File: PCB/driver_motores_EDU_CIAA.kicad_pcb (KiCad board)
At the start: 2 copper layers, 85 x 90 mm, 38 parts, among them P1 CONN_01X02, P2 CONN_01X04, P3 CONN_01X05, P4 CONN_01X05, Q1 AOD417, U1 PCA9685-TSSOP, U2 24C32, U3 TB6612FNG, U4 TB6612FNG

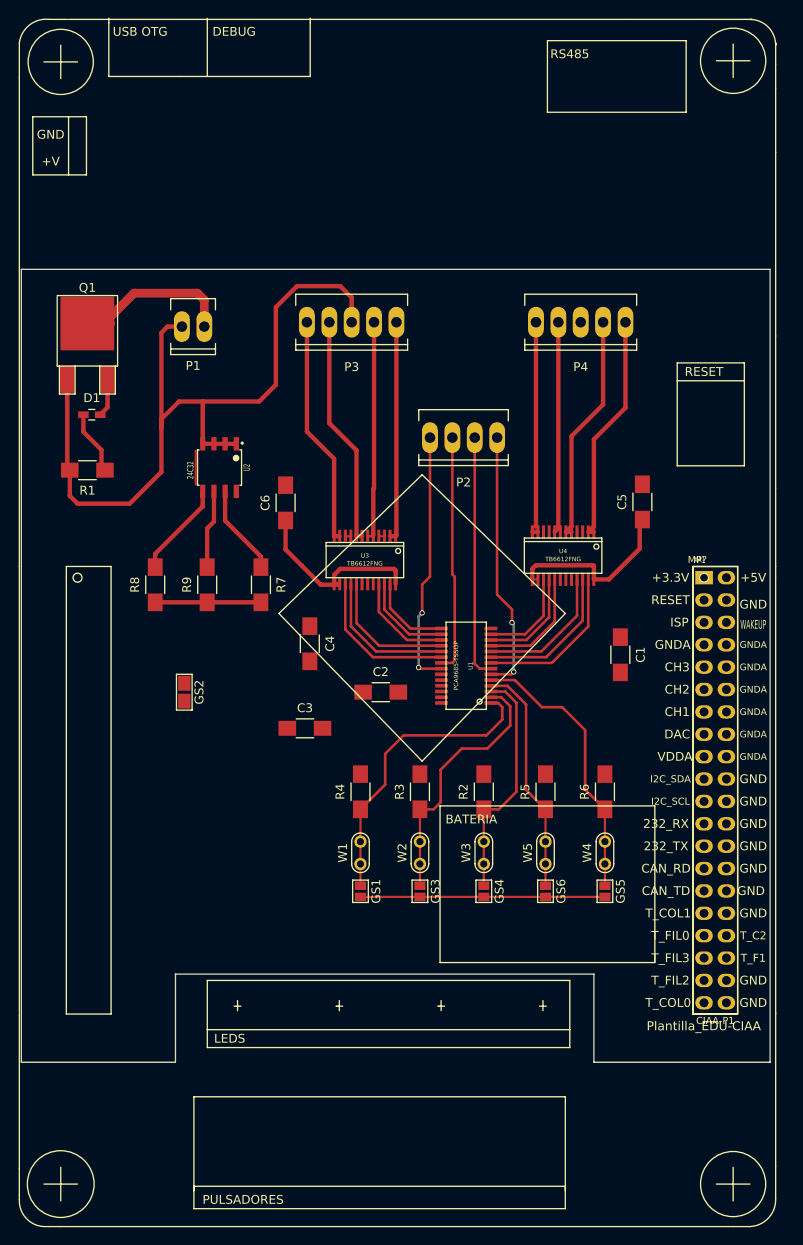
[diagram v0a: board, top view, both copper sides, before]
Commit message: termino ruteo, completo modulos 3D, modifico serigrafia
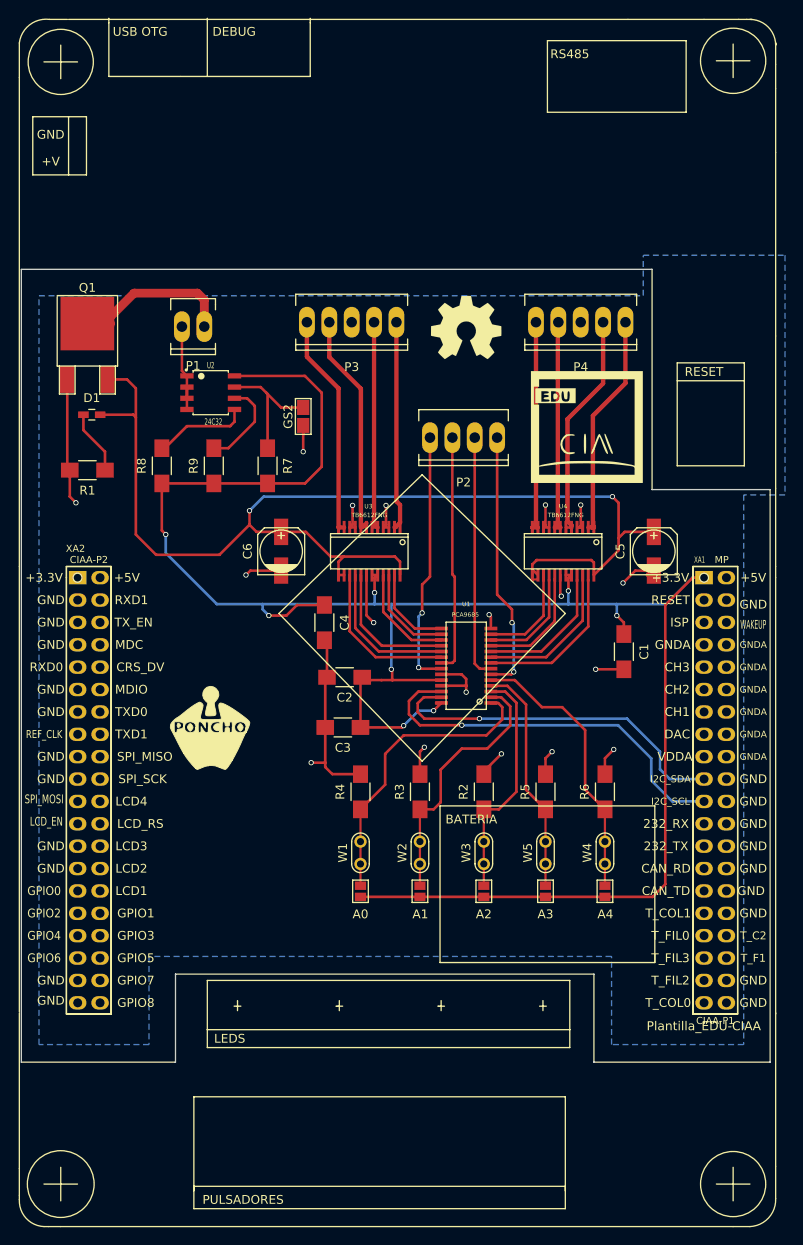
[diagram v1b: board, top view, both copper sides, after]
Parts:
- removed MP?: Plantilla_EDU-CIAA, ej2cese:Plantilla_EDU-CIAA
- added G***: LOGO, footprint:Logo_Poncho, F.Cu at (83.9, 107.1)
- added G***: Logo_EDU-CIAA, footprint:Logo_EDU-CIAA, F.Cu at (126.7, 72.9)
- added G101: Logo_OSHWA, footprint:Logo_OSHWA, F.Cu at (113.0, 61.6)
- added MP: Plantilla_EDU-CIAA, footprint:Plantilla_EDU-CIAA, F.Cu at (140.0, 90.0)
- added XA2: Conn_Poncho_Izquierdo, footprint:Conn_Poncho_Izquierdo, F.Cu at (68.9, 90.0)
- C5, C6: footprint tp_final:R_1206_HandSoldering -> Capacitors_SMD:c_elec_5x5.3
- U1: value PCA9685-TSSOP -> PCA9685
- moved GS2 34.1 mm to (94.5, 71.7), turned to 180 degrees
- moved R7 13.5 mm to (90.5, 77.3)
- moved R8 13.5 mm to (78.5, 77.3)
- moved R9 13.5 mm to (84.3, 77.3)
- moved U2 8.56 mm to (84.0, 69.0), turned to 0 degrees
- moved C5 5.75 mm to (134.3, 87.0)
- moved C6 5.52 mm to (92.0, 87.0)
- moved C2 4.44 mm to (99.2, 101.3), turned to 180 degrees
- moved C3 4.30 mm to (99.0, 107.0), turned to 180 degrees
- moved C4 2.91 mm to (96.9, 95.1)
- moved U3 1.12 mm to (102.0, 87.0)
- moved C1 0.53 mm to (130.9, 98.4)
- moved U4 0.50 mm to (124.0, 87.0)
- renumbered GS1 to A0, GS3 to A1, GS4 to A2, GS6 to A3, GS5 to A4
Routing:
- net +3V3: track 39.8 -> 238.7 mm, vias 0 -> 8
- net +12V: track 46.3 -> 131.9 mm, vias 0 -> 2
- net /SCL: track 0.00 -> 44.7 mm, vias 0 -> 1
- net /SDA: track 0.00 -> 40.8 mm, vias 0 -> 1
- net GND: track 93.5 -> 108.2 mm, vias 0 -> 18
- net Net-(GS2-Pad2): track 10.3 -> 15.4 mm
- net (no net): track 3.81 -> 0.00 mm
- net Net-(P3-Pad1): track 25.7 -> 23.8 mm
- net Net-(R9-Pad2): track 8.92 -> 10.4 mm
- net Net-(P3-Pad2): track 25.1 -> 24.2 mm
- net Net-(P3-Pad4): track 26.2 -> 25.4 mm
- net Net-(P3-Pad5): track 26.2 -> 25.4 mm
- net /LED11: track 15.2 -> 15.8 mm
- net /LED13: track 17.4 -> 18.0 mm
- net /LED12: track 16.3 -> 16.9 mm
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- added copper zone on B.Cu, net GND
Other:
- outline, holes or cut-outs redrawn

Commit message: se borran las carpetas sobrantes, completa el rotulo, se corrige el esquematico, se agrega serigrafia, se agrega tabla con las grillas
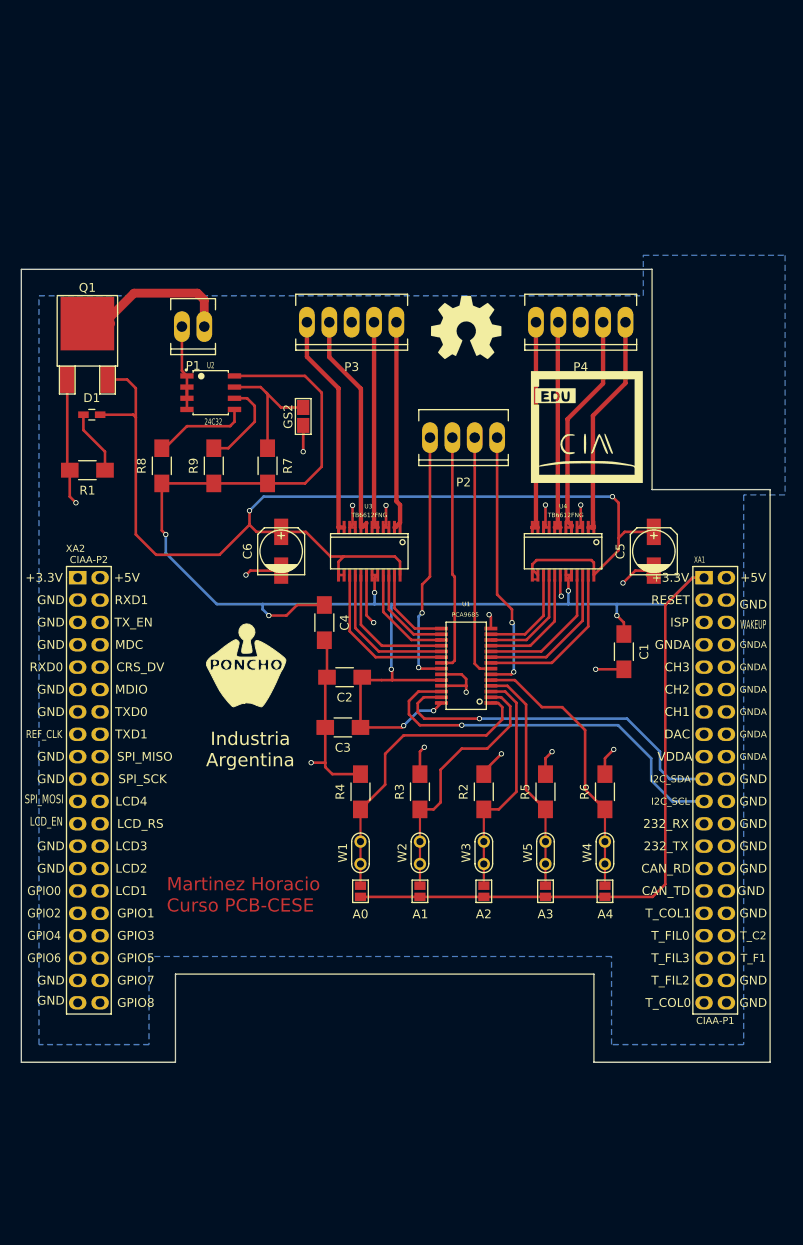
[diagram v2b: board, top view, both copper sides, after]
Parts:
- removed MP: Plantilla_EDU-CIAA, footprint:Plantilla_EDU-CIAA
- moved G*** 8.20 mm to (88.0, 100.0)
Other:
- net class Default: trace_width 0.25 -> 0.3; via_dia 0.6 -> 1.27; via_drill 0.4 -> 0.7
- net class net_power added: clearance 0.3, trace_width 0.75, via_dia 1.27, via_drill 0.7
- board text added: "Diseño doblefaz Sin requerimientos especiales Grilla de Ruteo: 0,1 mm Grilla de posicionamiento: 0,5 mm Ancho minimo de pista: 0,3 mm Diametro de agujero de via: 0,71 mm Diametro de via: 1,27mm"
- board text added: "Industria Argentina"
- board text added: "Martinez Horacio Curso PCB-CESE"
- board text added: "STACK-UP"

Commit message: se elimina carpeta DOC, se agregan serigrafias
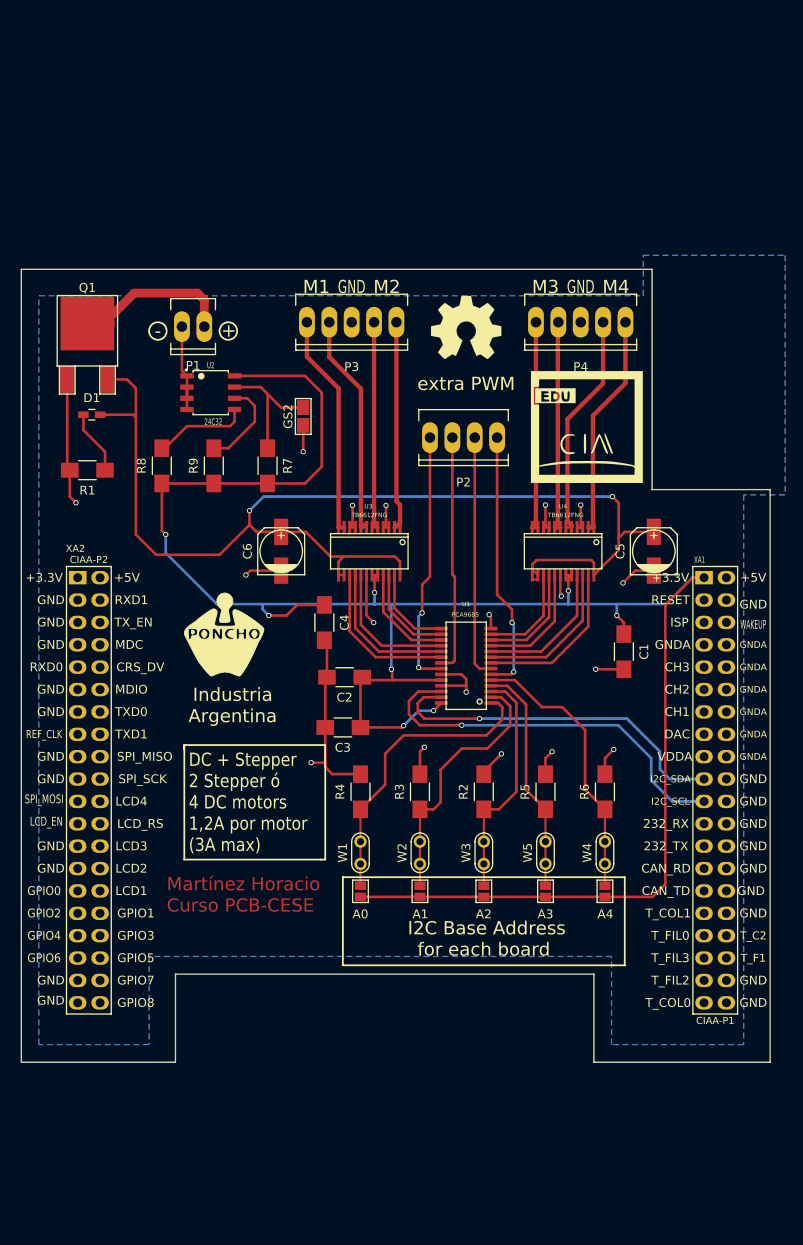
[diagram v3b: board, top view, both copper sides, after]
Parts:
- moved G*** 4.30 mm to (85.5, 96.5)
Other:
- board text added: "+"
- board text added: "-"
- board text added: "A cada tarjeta de la pila se le debe asignar una dirección única. Esto se hace con los puentes de dirección La dirección base I2C para cada tabla es 0x60."
- board text added: "DC + Stepper 2 Stepper ó 4 DC motors 1,2A por motor (3A max)"
- board text added: "GND"
- board text added: "I2C Base Address for each board"
- board text added: "M1"
- board text added: "M2"
- board text added: "M3"
- board text added: "M4"
- board text added: "Martínez Horacio Curso PCB-CESE"
- board text added: "extra PWM"
- board text removed: "Martinez Horacio Curso PCB-CESE"
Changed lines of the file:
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@@
     (area 62.424999 54.924999 147.575001 145.075001)
     (thickness 1.6)
-    (drawings 32)
+    (drawings 60)
     (tracks 391)
     (zones 0)
@@
       (effects (font (size 1 1) (thickness 0.15)))
     )
-    (fp_text value CONN_01X04 (at 0 5.08 180) (layer F.Fab)
+    (fp_text value CONN_01X04 (at -0.3 3.1 180) (layer F.Fab)
       (effects (font (size 1 1) (thickness 0.15)))
     )
@@
       (effects (font (size 1 1) (thickness 0.15)))
     )
-    (fp_text value TEST_1P (at 1.27 2 90) (layer F.Fab)
+    (fp_text value TEST_1P (at 1.27 2 90) (layer F.Fab) hide
       (effects (font (size 1 1) (thickness 0.15)))
     )
@@
       (effects (font (size 1 1) (thickness 0.15)))
     )
-    (fp_text value TEST_1P (at 1.27 2 90) (layer F.Fab)
+    (fp_text value TEST_1P (at 1.27 2 90) (layer F.Fab) hide
       (effects (font (size 1 1) (thickness 0.15)))
     )
@@
       (effects (font (size 1 1) (thickness 0.15)))
     )
-    (fp_text value TEST_1P (at 1.27 2 90) (layer F.Fab)
+    (fp_text value TEST_1P (at 1.27 2 90) (layer F.Fab) hide
       (effects (font (size 1 1) (thickness 0.15)))
     )
@@
       (effects (font (size 1 1) (thickness 0.15)))
     )
-    (fp_text value TEST_1P (at 1.27 2 90) (layer F.Fab)
+    (fp_text value TEST_1P (at 1.27 2 90) (layer F.Fab) hide
       (effects (font (size 1 1) (thickness 0.15)))
     )
@@
   )
   (module footprint:Logo_Poncho (layer F.Cu)
-    (at 88 100)
+    (at 85.5 96.5)
     (fp_text reference G*** (at 0.127 5.588) (layer F.SilkS) hide
       (effects (font (thickness 0.3)))
@@
     )
   )
-  (gr_text "Industria \nArgentina" (at 88.5 109.5) (layer F.SilkS)
+  (gr_text "extra PWM" (at 113 68) (layer F.SilkS)
     (effects (font (size 1.5 1.5) (thickness 0.3)))
   )
-  (gr_text "Martinez Horacio\nCurso PCB-CESE" (at 79 126) (layer F.Cu)
+  (gr_text GND (at 126 57) (layer F.SilkS)
+    (effects (font (size 1.5 1) (thickness 0.25)))
+  )
+  (gr_text GND (at 100 57) (layer F.SilkS)
+    (effects (font (size 1.5 1) (thickness 0.25)))
+  )
+  (gr_text M4 (at 130 57) (layer F.SilkS)
+    (effects (font (size 1.5 1.5) (thickness 0.3)))
+  )
+  (gr_text M3 (at 122 57) (layer F.SilkS)
+    (effects (font (size 1.5 1.5) (thickness 0.3)))
+  )
+  (gr_text M2 (at 104 57) (layer F.SilkS)
+    (effects (font (size 1.5 1.5) (thickness 0.3)))
+  )
+  (gr_text M1 (at 96 57) (layer F.SilkS)
+    (effects (font (size 1.5 1.5) (thickness 0.3)))
+  )
+  (gr_circle (center 78 62) (end 78 61) (layer F.SilkS) (width 0.2))
+  (gr_circle (center 86 62) (end 87 62) (layer F.SilkS) (width 0.2))
+  (gr_text - (at 78 62) (layer F.SilkS)
+    (effects (font (size 1.5 1.5) (thickness 0.3)))
+  )
+  (gr_text + (at 86 62 90) (layer F.SilkS)
+    (effects (font (size 1.5 1.5) (thickness 0.3)))
+  )
+  (gr_text "A cada tarjeta de la pila se le debe asignar una dirección única.\nEsto se hace con los puentes de dirección \nLa dirección base I2C para cada tabla es 0x60.\n" (at 197 95) (layer Dwgs.User)
     (effects (font (size 1.5 1.5) (thickness 0.3)) (justify left))
   )
+  (gr_text " I2C Base Address\nfor each board" (at 115 131) (layer F.SilkS)
+    (effects (font (size 1.5 1.5) (thickness 0.3)))
+  )
+  (gr_line (start 131 124) (end 99 124) (angle 90) (layer F.SilkS) (width 0.2))
+  (gr_line (start 131 134) (end 131 124) (angle 90) (layer F.SilkS) (width 0.2))
+  (gr_line (start 99 134) (end 131 134) (angle 90) (layer F.SilkS) (width 0.2))
+  (gr_line (start 99 124) (end 99 134) (angle 90) (layer F.SilkS) (width 0.2))
+  (gr_line (start 275 79) (end 195 79) (angle 90) (layer Dwgs.User) (width 0.2))
+  (gr_line (start 275 128) (end 275 79) (angle 90) (layer Dwgs.User) (width 0.2))
+  (gr_line (start 195 128) (end 275 128) (angle 90) (layer Dwgs.User) (width 0.2))
+  (gr_line (start 195 79) (end 195 128) (angle 90) (layer Dwgs.User) (width 0.2))
+  (gr_line (start 81 109) (end 81 109.5) (angle 90) (layer F.SilkS) (width 0.2))
+  (gr_line (start 97 109) (end 81 109) (angle 90) (layer F.SilkS) (width 0.2))
+  (gr_line (start 97 122) (end 97 109) (angle 90) (layer F.SilkS) (width 0.2))
+  (gr_line (start 96.5 122) (end 97 122) (angle 90) (layer F.SilkS) (width 0.2))
+  (gr_line (start 81 122) (end 96.5 122) (angle 90) (layer F.SilkS) (width 0.2))
+  (gr_line (start 81 109) (end 81 122) (angle 90) (layer F.SilkS) (width 0.2))
+  (gr_text "DC + Stepper\n2 Stepper ó \n4 DC motors\n1,2A por motor\n(3A max)" (at 81.5 115.5) (layer F.SilkS)
+    (effects (font (size 1.5 1.3) (thickness 0.3)) (justify left))
+  )
+  (gr_text "Industria \nArgentina" (at 86.5 104.5) (layer F.SilkS)
+    (effects (font (size 1.5 1.5) (thickness 0.3)))
+  )
+  (gr_text "Martínez Horacio\nCurso PCB-CESE" (at 79 126) (layer F.Cu)
+    (effects (font (size 1.5 1.5) (thickness 0.3)) (justify left))
+  )
